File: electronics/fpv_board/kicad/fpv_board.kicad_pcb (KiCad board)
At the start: 2 copper layers, 64.8 x 25.4 mm, 13 parts, among them K1 CONN_3, K2 CONN_3, K3 CONN_3, K4 CONN_3, P1 CONN_2, P2 CONN_2, SW1 SWITCH_INV, SW2 SWITCH_INV, SW3 4-SW_DIP, U1 LD1117DT33, U2 L78M05, U3 TX-5800-200

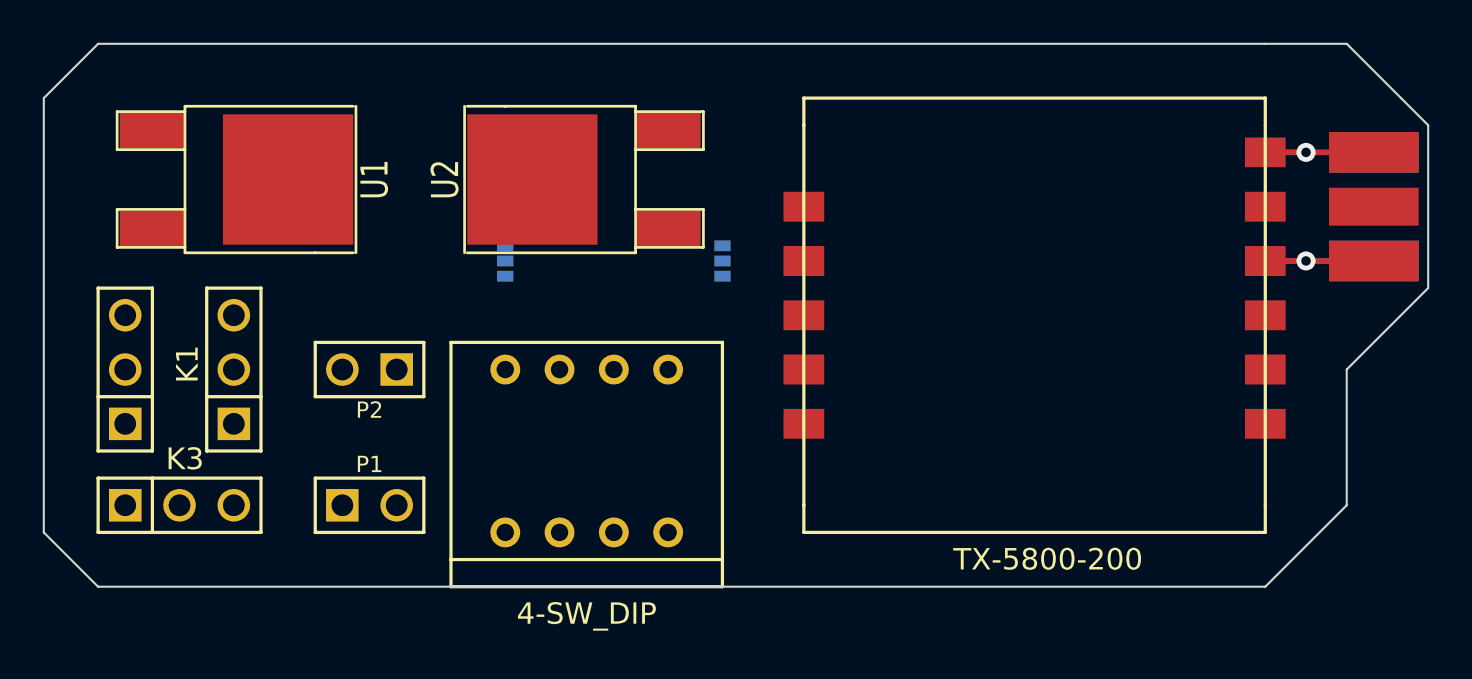
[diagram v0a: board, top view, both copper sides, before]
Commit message: Added 5V source selecter jumper to FPV board schematic. Implemented FPV PCB.
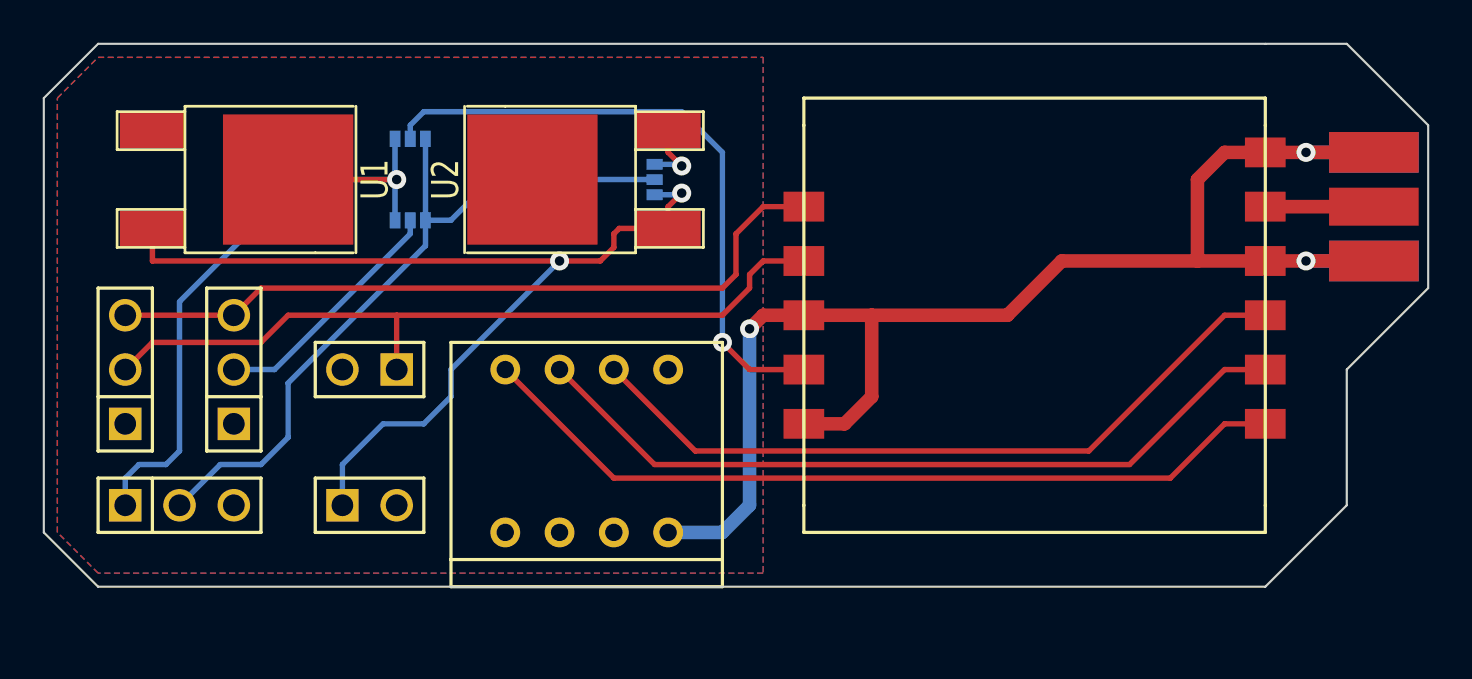
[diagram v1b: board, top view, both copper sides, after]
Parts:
- added SW4: SWITCH_INV, solder_jumper_3, B.Cu at (42.5, 20.3)
- moved SW2 15.7 mm to (31.1, 18.4), turned to 0 degrees
- moved SW1 4.84 mm to (31.1, 22.2), turned to 0 degrees
- renumbered K4 to KB4
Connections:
- U2 pad VO: +5V -> N-000007
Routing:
- net GND: track 20.3 -> 69.6 mm, vias 2 -> 3
- net /V++: track 0.00 -> 46.6 mm, vias 0 -> 2
- net N-000002: track 0.00 -> 38.7 mm
- net /AUDIO: track 0.00 -> 36.8 mm
- net N-000001: track 0.00 -> 36.7 mm
- net /VIDEO: track 0.00 -> 35.0 mm
- net N-000003: track 0.00 -> 34.7 mm
- net +5V: track 0.00 -> 34.5 mm
- net +3.3V: track 0.00 -> 32.9 mm, vias 0 -> 1
- net N-000009: track 0.00 -> 29.5 mm, vias 0 -> 1
- net N-0000011: track 0.00 -> 11.5 mm
- net N-000006: track 0.00 -> 5.08 mm
- net N-000007: track 0.00 -> 3.22 mm, vias 0 -> 1
- added copper zone on B.Cu, net GND
- added copper zone on F.Cu, net GND

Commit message: Added silkscreen labels to FPV PCB, also added additonal GND connection to Tx module.
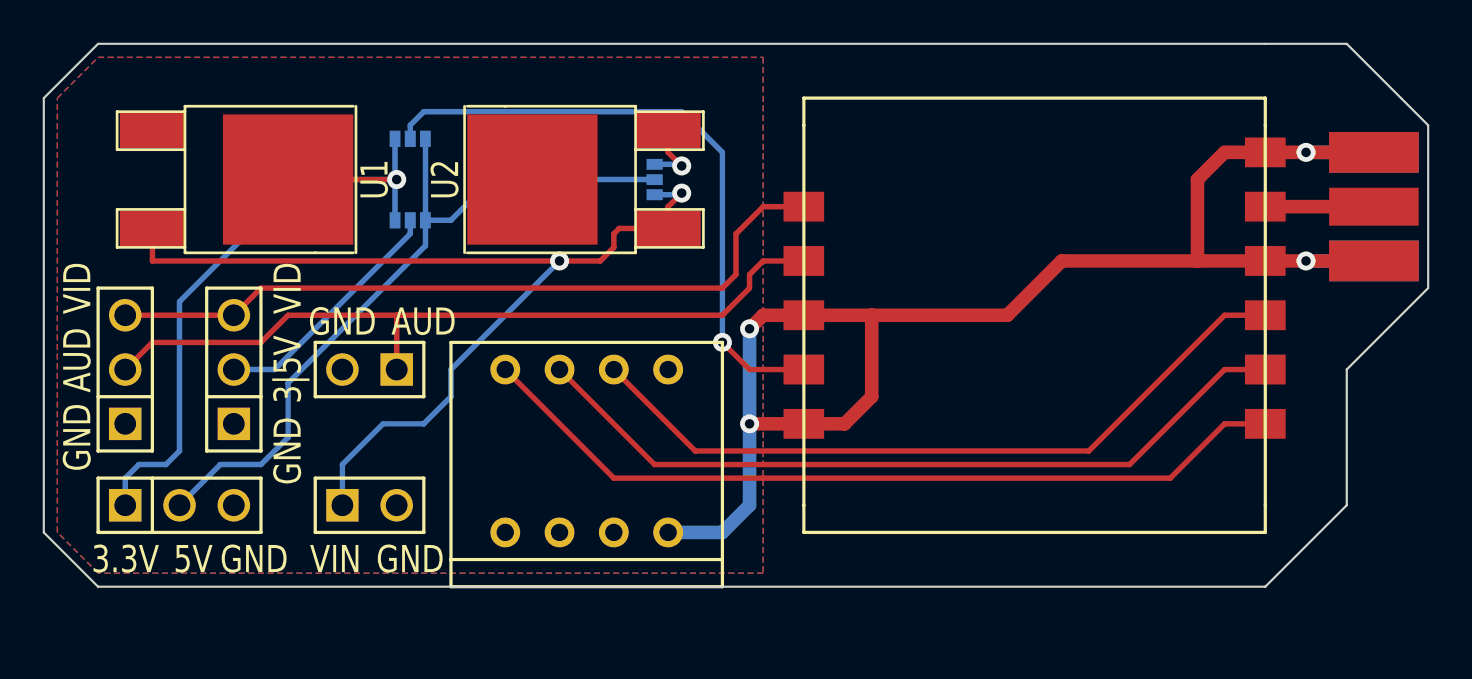
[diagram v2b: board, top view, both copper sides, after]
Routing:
- net GND: track 69.6 -> 72.1 mm, vias 3 -> 4
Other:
- board text added: "3.3V"
- board text added: "3|5V"
- board text added: "5V"
- board text added: "5V-REG"
- board text added: "AUD"
- board text added: "GND"
- board text added: "JMP1"
- board text added: "JMP2"
- board text added: "JMP3"
- board text added: "VID"
- board text added: "VIN"
- board text added: "ZÆRIK FPV BOARD REV 1.0 - MAY 2014 ZACHARY CLAPPER"
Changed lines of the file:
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@@
     (links 38)
     (no_connects 0)
-    (area 13.919999 13.919999 80.839 41.469)
+    (area 13.88231 13.919999 80.839 41.469)
     (thickness 1.6)
-    (drawings 12)
-    (tracks 114)
+    (drawings 33)
+    (tracks 117)
     (zones 0)
     (modules 14)
@@
   (page A3)
   (layers
-    (15 F.Cu signal)
+    (15 F.Cu signal hide)
     (0 B.Cu signal)
     (16 B.Adhes user)
@@
     (19 F.Paste user)
     (20 B.SilkS user)
-    (21 F.SilkS user)
+    (21 F.SilkS user hide)
     (22 B.Mask user)
     (23 F.Mask user)
@@
   )
   (setup
-    (last_trace_width 0.635)
+    (last_trace_width 0.254)
     (user_trace_width 0.635)
     (trace_clearance 0.254)
@@
     (pad_to_mask_clearance 0)
     (aux_axis_origin 0 0)
-    (visible_elements 7FFFFBBF)
+    (visible_elements 7FFFDABF)
     (pcbplotparams
       (layerselection 3178497)
@@
   (module solder_jumper_3 (layer B.Cu)
     (at 42.545 20.32 90)
-    (fp_text reference SW4 (at 0 1.905 90) (layer B.SilkS)
+    (fp_text reference SW4 (at 0 1.905 90) (layer B.SilkS) hide
       (effects (font (size 1 1) (thickness 0.15)) (justify mirror))
     )
@@
   (module solder_jumper_3 (layer B.Cu)
     (at 31.115 22.225)
-    (fp_text reference SW1 (at 0 1.905) (layer B.SilkS)
+    (fp_text reference SW1 (at 0 1.905) (layer B.SilkS) hide
       (effects (font (size 1 1) (thickness 0.15)) (justify mirror))
     )
@@
   (module solder_jumper_3 (layer B.Cu)
     (at 31.115 18.415)
-    (fp_text reference SW2 (at 0 1.905) (layer B.SilkS)
+    (fp_text reference SW2 (at 0 1.905) (layer B.SilkS) hide
       (effects (font (size 1 1) (thickness 0.15)) (justify mirror))
     )
@@
       (clearance 0.0254)
     )
+  )
+  (gr_text "ZÆRIK FPV BOARD\nREV 1.0 - MAY 2014\nZACHARY CLAPPER" (at 59.69 29.21) (layer B.SilkS)
+    (effects (font (size 1.5 1.5) (thickness 0.3)) (justify mirror))
+  )
+  (gr_text JMP3 (at 45.72 20.955 90) (layer B.SilkS)
+    (effects (font (size 1.27 1.016) (thickness 0.254)) (justify mirror))
+  )
+  (gr_text JMP2 (at 31.115 23.6855) (layer B.SilkS)
+    (effects (font (size 1.27 1.016) (thickness 0.254)) (justify mirror))
+  )
+  (gr_text JMP1 (at 31.115 17.145) (layer B.SilkS)
+    (effects (font (size 1.27 1.016) (thickness 0.254)) (justify mirror))
+  )
+  (gr_text 5V-REG (at 41.275 18.415) (layer B.SilkS)
+    (effects (font (size 1.27 1.016) (thickness 0.254)) (justify mirror))
+  )
+  (gr_text VIN (at 42.545 22.5425) (layer B.SilkS)
+    (effects (font (size 1.27 1.016) (thickness 0.254)) (justify mirror))
+  )
+  (gr_text 5V (at 33.02 20.32 90) (layer B.SilkS)
+    (effects (font (size 1.27 1.016) (thickness 0.254)) (justify mirror))
+  )
+  (gr_text 3.3V (at 29.21 20.32 90) (layer B.SilkS)
+    (effects (font (size 1.27 1.016) (thickness 0.254)) (justify mirror))
+  )
+  (gr_text 3|5V (at 25.4 29.21 90) (layer F.SilkS)
+    (effects (font (size 1.27 1.016) (thickness 0.254)))
+  )
+  (gr_text GND (at 27.94 26.9875) (layer F.SilkS)
+    (effects (font (size 1.27 1.016) (thickness 0.254)))
+  )
+  (gr_text 5V (at 20.955 38.1) (layer F.SilkS)
+    (effects (font (size 1.27 1.016) (thickness 0.254)))
+  )
+  (gr_text 3.3V (at 17.78 38.1) (layer F.SilkS)
+    (effects (font (size 1.27 1.016) (thickness 0.254)))
+  )
+  (gr_text VID (at 25.4 25.4 90) (layer F.SilkS)
+    (effects (font (size 1.27 1.016) (thickness 0.254)))
+  )
+  (gr_text GND (at 25.4 33.02 90) (layer F.SilkS)
+    (effects (font (size 1.27 1.016) (thickness 0.254)))
+  )
+  (gr_text GND (at 23.8125 38.1) (layer F.SilkS)
+    (effects (font (size 1.27 1.016) (thickness 0.254)))
+  )
+  (gr_text GND (at 15.5575 32.385 90) (layer F.SilkS)
+    (effects (font (size 1.27 1.016) (thickness 0.254)))
+  )
+  (gr_text AUD (at 15.5575 28.7655 90) (layer F.SilkS)
+    (effects (font (size 1.27 1.016) (thickness 0.254)))
+  )
+  (gr_text VID (at 15.5575 25.4 90) (layer F.SilkS)
+    (effects (font (size 1.27 1.016) (thickness 0.254)))
+  )
+  (gr_text VIN (at 27.6225 38.1) (layer F.SilkS)
+    (effects (font (size 1.27 1.016) (thickness 0.254)))
+  )
+  (gr_text GND (at 31.115 38.1) (layer F.SilkS)
+    (effects (font (size 1.27 1.016) (thickness 0.254)))
+  )
+  (gr_text AUD (at 31.75 26.9875) (layer F.SilkS)
+    (effects (font (size 1.27 1.016) (thickness 0.254)))
   )
   (gr_line (start 74.93 35.56) (end 71.12 39.37) (angle 90) (layer Edge.Cuts) (width 0.1))
@@
   (segment (start 47.625 21.59) (end 46.355 22.86) (width 0.254) (layer F.Cu) (net 5))
   (segment (start 22.86 26.67) (end 17.78 26.67) (width 0.254) (layer F.Cu) (net 5))
-  (segment (start 49.53 26.67) (end 47.625 26.67) (width 0.635) (layer F.Cu) (net 6) (status 400000))
-  (segment (start 45.72 36.83) (end 43.18 36.83) (width 0.635) (layer B.Cu) (net 6) (status 800000))
+  (segment (start 49.53 31.75) (end 46.99 31.75) (width 0.635) (layer F.Cu) (net 6))
+  (via (at 46.99 31.75) (size 0.889) (layers F.Cu B.Cu) (net 6))
+  (segment (start 49.53 26.67) (end 47.625 26.67) (width 0.635) (layer F.Cu) (net 6))
+  (segment (start 47.625 26.67) (end 46.99 27.305) (width 0.635) (layer F.Cu) (net 6))
+  (via (at 46.99 27.305) (size 0.889) (layers F.Cu B.Cu) (net 6))
+  (segment (start 46.99 27.305) (end 46.99 31.75) (width 0.635) (layer B.Cu) (net 6))
+  (segment (start 45.72 36.83) (end 43.18 36.83) (width 0.635) (layer B.Cu) (net 6))
+  (segment (start 46.99 31.75) (end 46.99 35.56) (width 0.635) (layer B.Cu) (net 6))
   (segment (start 46.99 35.56) (end 45.72 36.83) (width 0.635) (layer B.Cu) (net 6))
-  (segment (start 46.99 27.305) (end 46.99 35.56) (width 0.635) (layer B.Cu) (net 6))
-  (via (at 46.99 27.305) (size 0.889) (layers F.Cu B.Cu) (net 6))
-  (segment (start 47.625 26.67) (end 46.99 27.305) (width 0.635) (layer F.Cu) (net 6))
   (segment (start 49.53 31.75) (end 51.435 31.75) (width 0.635) (layer F.Cu) (net 6))
   (segment (start 52.705 30.48) (end 52.705 26.67) (width 0.635) (layer F.Cu) (net 6))
